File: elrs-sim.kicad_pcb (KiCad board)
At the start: 4 copper layers, 63.5 x 14 mm, 68 parts, among them IC1 SX1280IMLTRT, IC2 ESP8285, J1 Conn_01x04, J10 ESP_TX, J11 GND, J12 3.3V, J13 DP, J14 DN, J2 Conn_01x04, J3 Conn_01x04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

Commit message: Update main board
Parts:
- added C23: 1nF, Capacitor_SMD:C_0402_1005Metric, F.Cu at (154.1, 105.7)
- C12: value 100nF -> 1uF
- moved X3 0.95 mm to (152.0, 105.4)
- moved C7 0.17 mm to (155.4, 105.7)
- moved C8 0.17 mm to (156.5, 105.7)
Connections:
- X3 pad 3: Net-(IC1-XTA) -> Net-(X3-OUT)
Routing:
- net Net-(IC1-XTA): track 3.01 -> 1.19 mm
- net NSS: track 11.8 -> 13.5 mm
- net Net-(X3-OUT): track 0.00 -> 1.50 mm
- net GND: track 3.31 -> 2.33 mm
- net IRS: track 11.4 -> 10.8 mm
- net +3.3V_SW: track 54.4 -> 53.8 mm
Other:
- board text added: "ELRS Sim Stick V 0.0.1"
- board text removed: "Avolo"
- board text removed: "ELRS Sim Stick"
- board text removed: "v0.0.1"

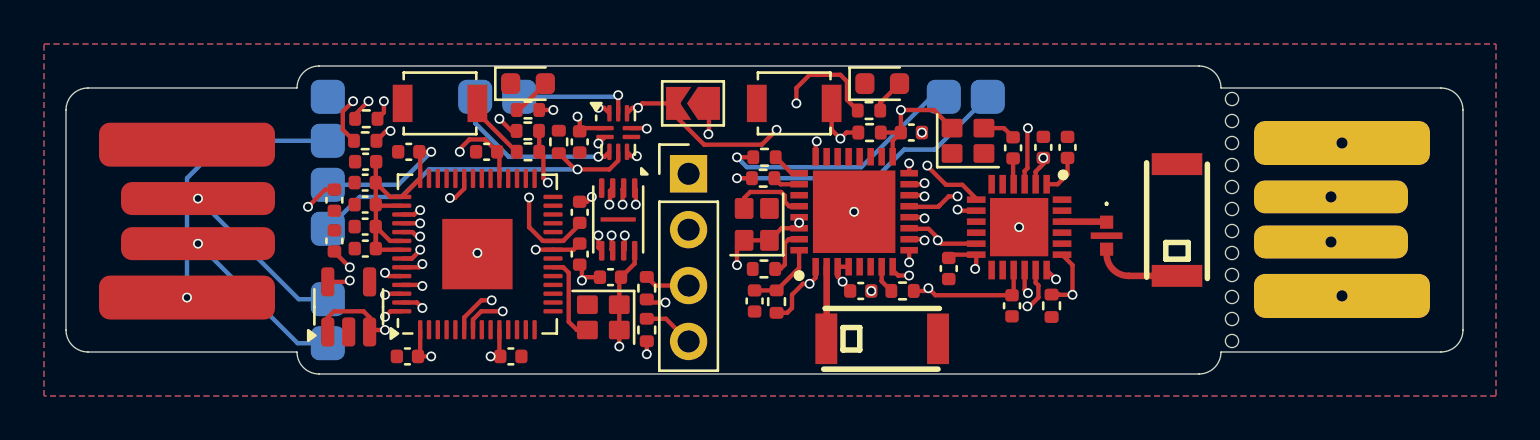
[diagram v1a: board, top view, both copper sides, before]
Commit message: Update: larger tolerances, better board shape
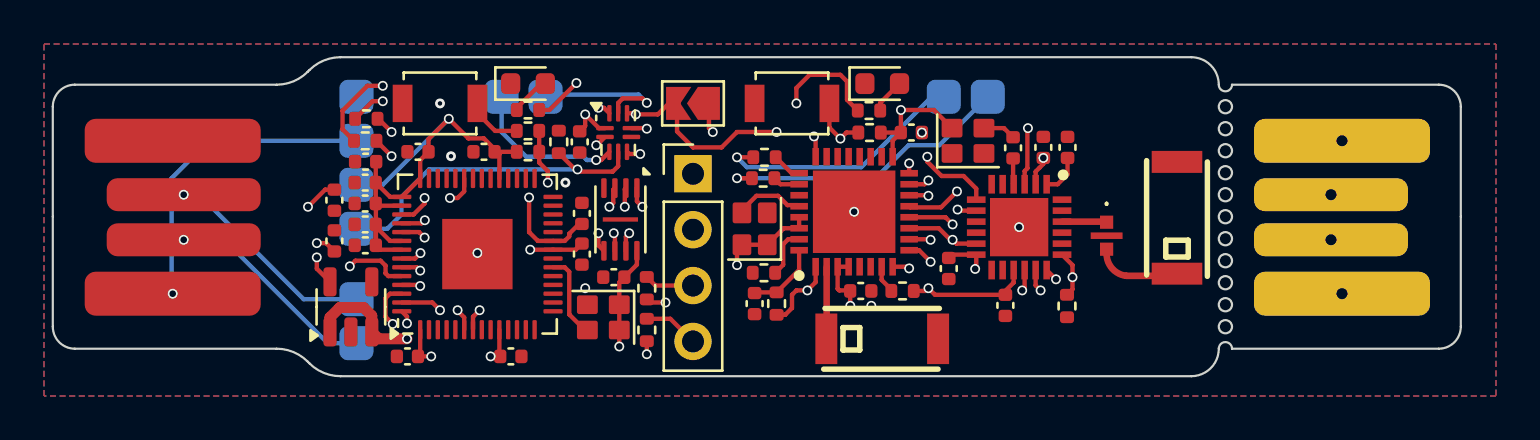
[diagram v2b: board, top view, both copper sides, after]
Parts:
- moved J11 1.30 mm to (124.2, 103.4)
- moved J12 1.30 mm to (124.2, 107.4)
- moved J13 1.30 mm to (124.2, 112.6)
- moved J14 1.30 mm to (124.2, 114.6)
- moved J4 1.30 mm to (124.2, 105.4)
- moved J6 1.30 mm to (124.2, 109.4)
- moved J7 1.20 mm to (130.8, 103.4)
- moved J8 1.20 mm to (132.8, 103.4)
- moved R12 0.95 mm to (132.0, 105.9)
- moved R10 0.95 mm to (132.0, 105.0)
- moved R2 0.70 mm to (156.5, 112.9)
- moved J1 0.67 mm to (119.9, 108.9)
- moved C17 0.42 mm to (127.0, 105.9)
- moved C6 0.30 mm to (153.7, 112.9)
- moved X2 0.22 mm to (142.3, 109.4)
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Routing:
- net USB_DP: track 19.3 -> 24.8 mm
- net QSPI_SCLK: track 13.2 -> 17.8 mm
- net USB_VBUS: track 42.8 -> 46.6 mm
- net USB_DN: track 19.7 -> 23.1 mm
- net RP2040_LED: track 8.32 -> 11.5 mm
- net +3.3V: track 37.8 -> 40.9 mm, vias 10 -> 8
- net RP2040_RX_NO: track 27.4 -> 24.5 mm
- net Net-(U1-VREG_VOUT): track 25.7 -> 28.1 mm
- net GND: track 2.33 -> 0.05 mm, vias 7 -> 9
- net ESP_MOSI: track 10.6 -> 8.66 mm
- net Net-(U1-USB_DM): track 8.86 -> 7.12 mm
- net NSS: track 13.5 -> 12.1 mm
- net QSPI_SD2: track 14.7 -> 16.1 mm
- net ESP_MISO: track 8.31 -> 7.13 mm
- net RP2040_TX: track 25.1 -> 26.2 mm
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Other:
- board size 63.5 x 14 mm -> 64 x 14.5 mm

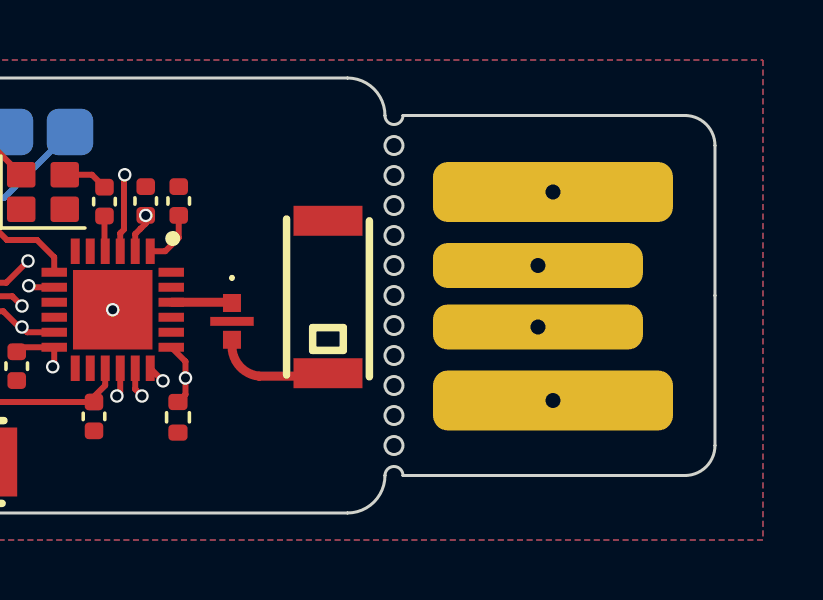
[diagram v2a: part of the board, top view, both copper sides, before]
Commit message: Update: Smooth out antenna traces
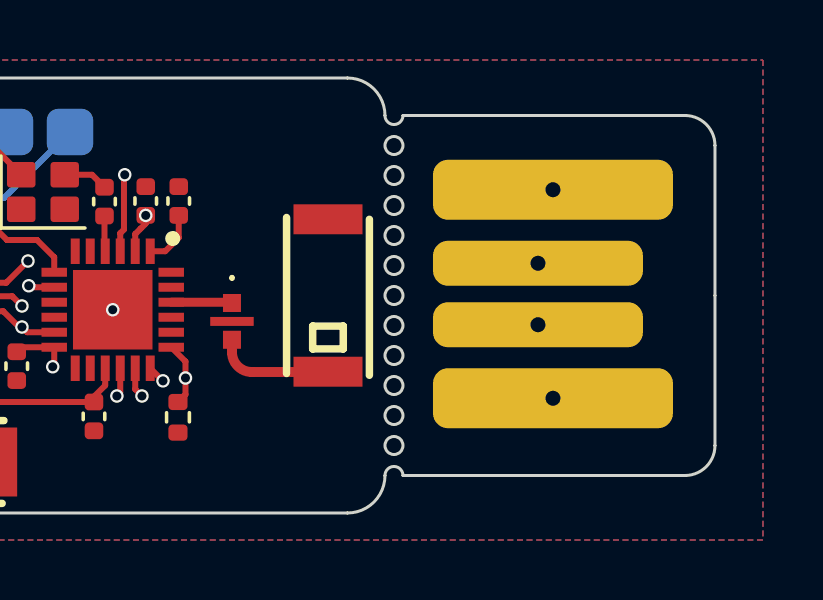
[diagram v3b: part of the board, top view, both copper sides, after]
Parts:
- moved J3 0.07 mm to (164.9, 108.8)
- moved L1 0.05 mm to (161.5, 108.8)
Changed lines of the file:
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@@
 			(pinfunction "OUT_(TO_ANTENNA)")
 			(pintype "passive")
+			(teardrops
+				(best_length_ratio 0.5)
+				(max_length 1)
+				(best_width_ratio 1)
+				(max_width 2)
+				(curve_points 5)
+				(filter_ratio 0.9)
+				(enabled yes)
+				(allow_two_segments yes)
+				(prefer_zone_connections yes)
+			)
 		)
 		(model "${KICAD8_3DMODEL_DIR}/Filter.3dshapes/Filter_Mini-Circuits_FV1206.wrl"
@@
 			(pinfunction "ANT")
 			(pintype "unspecified")
+			(teardrops
+				(best_length_ratio 0.5)
+				(max_length 1)
+				(best_width_ratio 1)
+				(max_width 2)
+				(curve_points 5)
+				(filter_ratio 0.9)
+				(enabled yes)
+				(allow_two_segments yes)
+				(prefer_zone_connections yes)
+			)
 		)
 		(pad "2" smd rect
@@
 	(footprint "CustomFootprints:PCB_USB_connector_top"
 		(layer "F.Cu")
-		(at 164.95 108.85 -90)
+		(at 164.95 108.775 -90)
 		(descr "USB pcb edge connector")
 		(tags "usb pcb edge connector")
@@
 	(footprint "easyeda2kicad:ANT-SMD_L5.2-W2.1"
 		(layer "F.Cu")
-		(at 161.5 108.9 90)
+		(at 161.5 108.85 90)
 		(property "Reference" "L1"
 			(at 0 -4 90)
@@
 			(pinfunction "ANT")
 			(pintype "unspecified")
+			(teardrops
+				(best_length_ratio 0.5)
+				(max_length 1)
+				(best_width_ratio 1)
+				(max_width 2)
+				(curve_points 5)
+				(filter_ratio 0.9)
+				(enabled yes)
+				(allow_two_segments yes)
+				(prefer_zone_connections yes)
+			)
 		)
 		(pad "2" smd rect
@@
 	(segment
 		(start 158.3 110.326)
-		(end 158.3 110.54)
-		(width 0.3)
+		(end 158.3 110.74)
+		(width 0.33)
 		(layer "F.Cu")
 		(net 1)
 	)
 	(segment
-		(start 161.402047 111.537953)
-		(end 161.5 111.44)
-		(width 0.3)
+		(start 158.96 111.4)
+		(end 161.49 111.4)
+		(width 0.33)
 		(layer "F.Cu")
 		(net 1)
 	)
 	(segment
-		(start 159.20171 111.537953)
-		(end 161.402047 111.537953)
-		(width 0.3)
+		(start 161.49 111.4)
+		(end 161.5 111.39)
+		(width 0.33)
 		(layer "F.Cu")
 		(net 1)
 	)
 	(arc
-		(start 158.3 110.54)
-		(mid 158.559049 111.211559)
-		(end 159.20171 111.537953)
-		(width 0.3)
+		(start 158.3 110.74)
+		(mid 158.49331 111.20669)
+		(end 158.96 111.4)
+		(width 0.33)
 		(layer "F.Cu")
 		(net 1)
@@
 	)
 	(zone
+		(net 23)
+		(net_name "LNA")
+		(layer "F.Cu")
+		(name "$teardrop_padvia$")
+		(hatch full 0.1)
+		(priority 30000)
+		(attr
+			(teardrop
+				(type padvia)
+			)
+		)
+		(connect_pads yes
+			(clearance 0)
+		)
+		(min_thickness 0.0254)
+		(filled_areas_thickness no)
+		(fill yes
+			(thermal_gap 0.5)
+			(thermal_bridge_width 0.5)
+			(island_removal_mode 1)
+			(island_area_min 10)
+		)
+		(polygon
+			(pts
+				(xy 145.425 112.75) (xy 145.354087 112.886777) (xy 145.283174 113.005165) (xy 145.212262 113.105165)
+				(xy 145.141349 113.186777) (xy 145.070437 113.25) (xy 145.56 114.401) (xy 146.06 113.25) (xy 145.992999 113.18611)
+				(xy 145.925999 113.104166) (xy 145.859 113.004166) (xy 145.792 112.88611) (xy 145.725 112.75)
+			)
+		)
+	)
+	(zone
+		(net 1)
+		(net_name "Net-(ANT1-OUT_(TO_ANTENNA))")
+		(layer "F.Cu")
+		(name "$teardrop_padvia$")
+		(hatch full 0.1)
+		(priority 30002)
+		(attr
+			(teardrop
+				(type padvia)
+			)
+		)
+		(connect_pads yes
+			(clearance 0)
+		)
+		(min_thickness 0.0254)
+		(filled_areas_thickness no)
+		(fill yes
+			(thermal_gap 0.5)
+			(thermal_bridge_width 0.5)
+			(island_removal_mode 1)
+			(island_area_min 10)
+		)
+		(polygon
+			(pts
+				(xy 158.462419 110.777474) (xy 158.489935 110.734901) (xy 158.517451 110.698468) (xy 158.544967 110.668173)
+				(xy 158.572483 110.644017) (xy 158.6 110.626) (xy 158.299778 110.325026) (xy 158.00087 110.626)
+				(xy 158.028834 110.655091) (xy 158.056799 110.692127) (xy 158.084763 110.737108) (xy 158.112728 110.790033)
+				(xy 158.140693 110.850904)
+			)
+		)
+	)
+	(zone
+		(net 1)
+		(net_name "Net-(ANT1-OUT_(TO_ANTENNA))")
+		(layer "F.Cu")
+		(name "$teardrop_padvia$")
+		(hatch full 0.1)
+		(priority 30001)
+		(attr
+			(teardrop
+				(type padvia)
+			)
+		)
+		(connect_pads yes
+			(clearance 0)
+		)
+		(min_thickness 0.0254)
+		(filled_areas_thickness no)
+		(fill yes
+			(thermal_gap 0.5)
+			(thermal_bridge_width 0.5)
+			(island_removal_mode 1)
+			(island_area_min 10)
+		)
+		(polygon
+			(pts
+				(xy 159.85 111.565) (xy 159.95 111.594219) (xy 160.05 111.641329) (xy 160.149999 111.706329) (xy 160.249999 111.789219)
+				(xy 160.35 111.89) (xy 161.501 111.39) (xy 160.35 110.896962) (xy 160.249999 111.000782) (xy 160.149999 111.086496)
+				(xy 160.05 111.154103) (xy 159.95 111.203605) (xy 159.85 111.235)
+			)
+		)
+	)
+	(zone
